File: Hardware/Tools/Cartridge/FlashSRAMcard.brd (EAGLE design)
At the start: 47.9 x 47.9 mm, 18 parts, among them IC1 AS29CF160B-55TIN, IC2 74LS595D, IC3 74LS244DW, IC5 74AHC1G04DBV, IC6 74AHC1G32DBV, IC7 74AHC1G32DBV

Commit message: more sram cart changes
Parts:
- removed VCC: 74AHC1G04DBV, 74xx-little-us:SOT23-5
- added D1, D2: (no value), semicon-smd-ipc:MELF-MLL34
- added IC4: 74AHC1G04DBV, 74xx-little-us:SOT23-5
- added R1, R2, R3: (no value), rcl:R0805
- added U$3: BATTERY2025-SMD, 0_gametankparts:CR2025-SMD
- IC2: value 74LS595D -> 74HC595; device 74xx-us:SO16 -> 0_gametankparts:TSSOP16
- IC3: value 74LS244DW -> 74HC244; device 74xx-us:SO20W -> 0_gametankparts:TSSOP20
- U$2: value SRAM_32KSOP28 -> SRAM_32KTSOP28; device 0_gametankparts:SO28-3 -> 0_gametankparts:TSOP10X14
- moved C3 34.5 mm to (43.2, 30.5)
- moved IC2 33.9 mm to (41.9, 26.7)
- moved C4 22.6 mm to (1.78, 12.1), turned to 270 degrees
- moved IC5 18.1 mm to (7.62, 26.7)
- moved C5 18.1 mm to (7.49, 29.6)
- moved C7 18.1 mm to (7.49, 23.2)
- moved C8 16.6 mm to (16.4, 23.2)
- moved C6 16.6 mm to (16.5, 29.6)
- moved IC6 16.6 mm to (16.5, 20.3)
- moved IC7 16.6 mm to (16.5, 26.7)
- moved C2 15.3 mm to (30.5, 24.1)
- moved IC3 12.5 mm to (25.4, 25.4)
- moved U$2 6.48 mm to (11.4, 12.7)
- moved W 4.58 mm to (27.9, 12.7)
- moved IC1 2.84 mm to (33.0, 14.0)
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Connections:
- new net N$5: D1.2, U$3.P$1
- new net N$6: C4.1, D1.1, D2.1, R1.1, R2.1, R3.1, U$2.7
- net !BANKING: now also IC4.2; no longer VCC.2
- net !OE: now also R1.2, U$2.1; no longer U$2.22
- net !WE: now also R2.2, U$2.6; no longer U$2.27
- net A-1: now also U$2.17; no longer U$2.10
- net A0: now also U$2.16; no longer U$2.9
- net A1: now also U$2.15; no longer U$2.8
- net A10: now also U$2.2; no longer U$2.23
- net A11: now also U$2.9; no longer U$2.2
- net A12: now also U$2.5; no longer U$2.26
- net A2: now also U$2.14; no longer U$2.7
- net A3: now also U$2.13; no longer U$2.6
- net A4: now also U$2.12; no longer U$2.5
- net A5: now also U$2.11; no longer U$2.4
- net A6: now also U$2.10; no longer U$2.3
- net A7: now also U$2.4; no longer U$2.25
- net A8: now also U$2.3; no longer U$2.24
- net A9: now also U$2.28; no longer U$2.21
- net D0: now also U$2.18
- net D1: now also U$2.19
- net D2: now also U$2.20
- net D3: now also U$2.22
- net D4: now also U$2.23
- net D5: now also U$2.24
- net D6: now also U$2.25
- net D7: now also U$2.26
- net GND: now also IC4.3, U$2.21, U$3.P$2; no longer U$2.14, VCC.3
- net N$1: now also IC4.4; no longer VCC.4
- net N$2: now also R3.2, U$2.27; no longer U$2.20
- net VCC: now also D2.2, IC4.5; no longer C4.1, U$2.28, VCC.5
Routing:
- net A17: track 92.6 -> 31.5 mm, vias 0 -> 3
- net BANK_DONE: track 37.2 -> 97.1 mm, vias 2 -> 0
- net GND: track 43.2 -> 97.1 mm, vias 14 -> 17
- net A15: track 70.9 -> 25.9 mm, vias 0 -> 2
- net N$6: track 0.00 -> 41.3 mm, vias 0 -> 1
- net A18: track 67.1 -> 31.2 mm, vias 4 -> 3
- net A14: track 63.3 -> 28.2 mm, vias 3 -> 2
- net N$1: track 24.2 -> 58.0 mm
- net !BANKING: track 45.8 -> 79.2 mm
- net !RESET: track 76.3 -> 42.9 mm
- net A-1: track 81.3 -> 48.3 mm, vias 4 -> 3
- net A16: track 52.8 -> 22.4 mm
- net BANK_CLK: track 46.3 -> 73.4 mm, vias 0 -> 2
- net A19: track 58.6 -> 35.8 mm
- net !WE: track 50.2 -> 72.8 mm, vias 4 -> 2
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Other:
- board text removed: "74HC1G04"
- board text removed: "74HC1G32"
- board text removed: "74HC244"
- board text removed: "74HC595"
- board text removed: "FLASH"
- board text removed: "RAM"

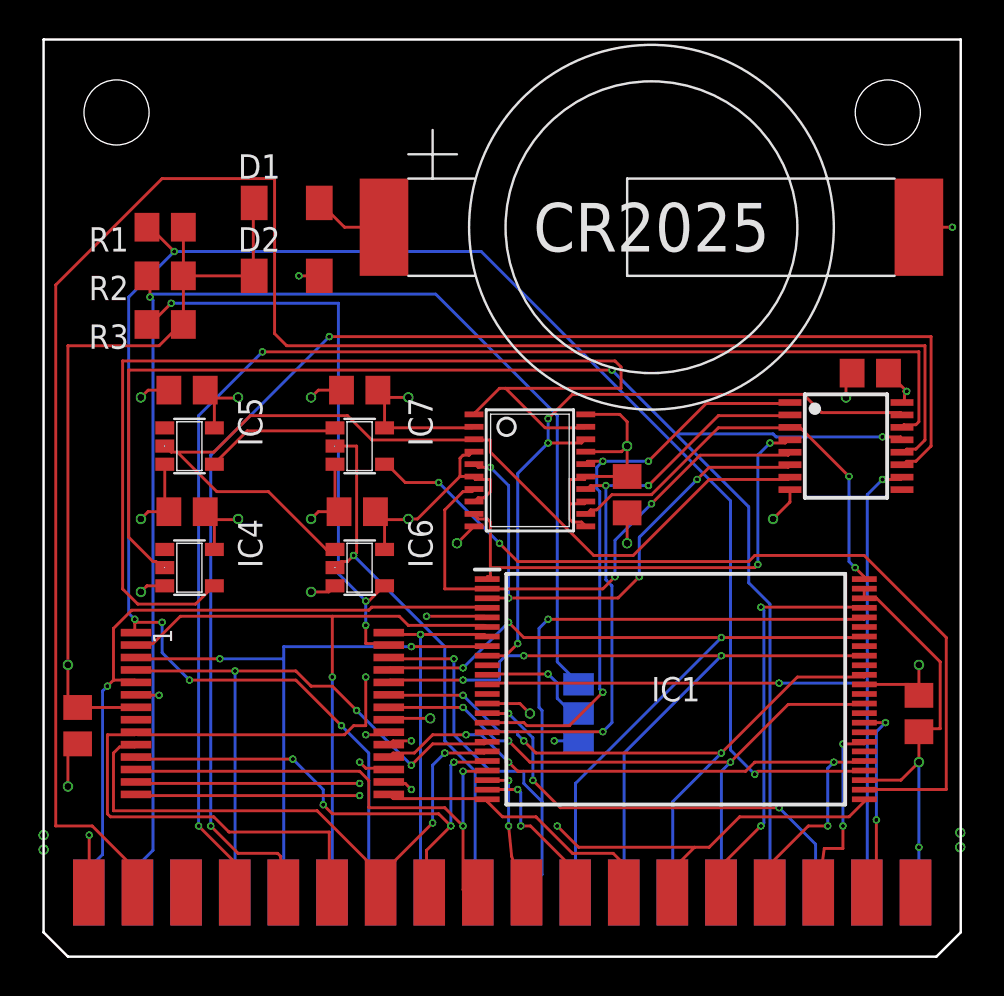
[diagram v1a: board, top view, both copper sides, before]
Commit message: RAM cartridge fixes
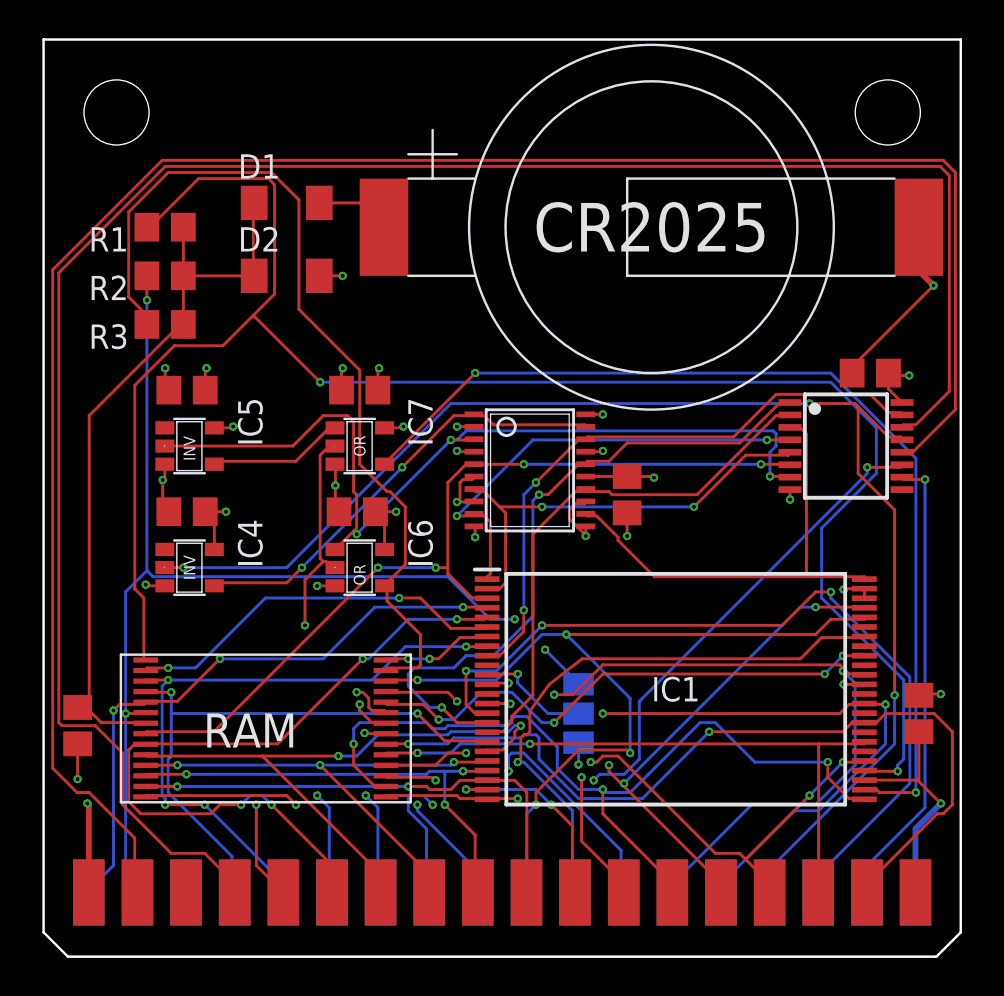
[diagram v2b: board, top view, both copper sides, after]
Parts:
- U$2: value SRAM_32KTSOP28 -> SRAM_32KALLIANCE; device 0_gametankparts:TSOP10X14 -> 0_gametankparts:STSOP28
- moved U$2 1.05 mm to (11.7, 11.7), turned to 0 degrees
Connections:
- removed net N$6: C4.1, D1.1, D2.1, R1.1, R2.1, R3.1, U$2.7
- new net V_SRAM: C4.1, D1.1, D2.1, R1.1, R2.1, R3.1, U$2.P6
- net !OE: now also U$2.P0; no longer U$2.1
- net !WE: now also U$2.P5; no longer U$2.6
- net A-1: now also U$2.P16; no longer U$2.17
- net A0: now also U$2.P15; no longer U$2.16
- net A1: now also U$2.P14; no longer U$2.15
- net A10: now also U$2.P1; no longer U$2.2
- net A11: now also U$2.P8; no longer U$2.9
- net A12: now also U$2.P4; no longer U$2.5
- net A13: now also U$2.P7
- net A2: now also U$2.P13; no longer U$2.14
- net A3: now also U$2.P12; no longer U$2.13
- net A4: now also U$2.P11; no longer U$2.12
- net A5: now also U$2.P10; no longer U$2.11
- net A6: now also U$2.P9; no longer U$2.10
- net A7: now also U$2.P3; no longer U$2.4
- net A8: now also U$2.P2; no longer U$2.3
- net A9: now also U$2.P27; no longer U$2.28
- net D0: now also U$2.P17; no longer U$2.18
- net D1: now also U$2.P18; no longer U$2.19
- net D2: now also U$2.P19; no longer U$2.20
- net D3: now also U$2.P21; no longer U$2.22
- net D4: now also U$2.P22; no longer U$2.23
- net D5: now also U$2.P23; no longer U$2.24
- net D6: now also U$2.P24; no longer U$2.25
- net D7: now also U$2.P25; no longer U$2.26
- net GND: now also U$2.P20; no longer U$2.21
- net N$2: now also U$2.P26; no longer U$2.27
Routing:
- net VCC: track 105.8 -> 37.7 mm, vias 13 -> 20
- net GND: track 97.1 -> 38.6 mm, vias 17 -> 14
- net N$6: track 41.3 -> 0.00 mm, vias 1 -> 0
- net V_SRAM: track 0.00 -> 39.5 mm
- net N$1: track 58.0 -> 23.4 mm, vias 0 -> 2
- net BANK_SER: track 69.4 -> 101.8 mm, vias 2 -> 0
- net !OE: track 101.6 -> 129.8 mm, vias 6 -> 3
- net BANK_CLK: track 73.4 -> 49.0 mm, vias 2 -> 3
- net READY: track 23.9 -> 43.2 mm
- net A13: track 28.1 -> 45.0 mm
- net N$2: track 31.4 -> 46.5 mm, vias 3 -> 0
- net A0: track 30.2 -> 44.1 mm, vias 2 -> 3
- net !WE: track 72.8 -> 59.0 mm, vias 2 -> 4
- net D4: track 36.3 -> 47.6 mm
- net D3: track 34.3 -> 44.6 mm
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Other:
- board text added: "INV"
- board text added: "OR"
- board text added: "RAM"
- board text added: "RAM Cartridge v2 for GameTank 2MB Flash 32K RAM December 2022 Clyde Shaffer"

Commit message: some SRAM cartridge stuff
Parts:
- removed W: (no value), jumper:SJ_2
- added D3, D4, D5: (no value), semicon-smd-ipc:MELF-MLL34
- moved C5 3.81 mm to (3.68, 29.6)
- moved C7 3.81 mm to (3.68, 23.2)
- moved IC4 3.81 mm to (3.81, 20.3)
- moved IC5 3.81 mm to (3.81, 26.7)
- moved D1 2.84 mm to (11.4, 36.8)
- moved D2 2.84 mm to (11.4, 33.0)
- moved IC2 2.54 mm to (41.9, 24.1)
- moved C3 2.54 mm to (43.2, 27.9)
- moved IC3 1.80 mm to (26.7, 24.1)
- moved C2 1.80 mm to (31.8, 22.9)
- moved C4 1.27 mm to (1.78, 13.3)
- moved C6 1.27 mm to (17.8, 29.6)
- moved C8 1.27 mm to (17.7, 23.2)
- moved IC6 1.27 mm to (17.8, 20.3)
- moved IC7 1.27 mm to (17.8, 26.7)
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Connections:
- removed net N$3: IC1.11, W.2
- new net N$6: D3.2, IC6.4
- new net N$7: D4.1, R2.2, U$2.P5
- new net N$8: D5.1, R1.2, U$2.P0
- net !OE: now also D5.2; no longer R1.2, U$2.P0
- net !WE: now also D4.2, IC1.11; no longer R2.2, U$2.P5, W.1
- net N$2: now also D3.1; no longer IC6.4
- net VCC: no longer W.3
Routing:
- net GND: track 38.6 -> 170.4 mm, vias 14 -> 6
- net VCC: track 37.7 -> 143.7 mm, vias 20 -> 4
- net !OE: track 129.8 -> 46.8 mm
- net N$7: track 0.00 -> 31.4 mm
- net N$8: track 0.00 -> 30.3 mm, vias 0 -> 2
- net A5: track 26.9 -> 53.9 mm
- net BANK_SER: track 101.8 -> 77.3 mm, vias 0 -> 2
- net !WE: track 59.0 -> 38.3 mm, vias 4 -> 3
- net READY: track 43.2 -> 22.6 mm, vias 3 -> 2
- net BANK_CLK: track 49.0 -> 69.5 mm, vias 3 -> 2
- net A10: track 36.0 -> 52.8 mm
- net !CS: track 29.2 -> 45.4 mm
- net !BANKING: track 71.7 -> 85.1 mm
- net N$2: track 46.5 -> 34.4 mm, vias 0 -> 3
- net BANK_DONE: track 100.6 -> 89.2 mm, vias 0 -> 2
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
